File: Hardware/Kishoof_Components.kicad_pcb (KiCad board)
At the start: 2 copper layers, 76 parts, among them J1 SWD_Header, J2 Eurorack_10_pin_power, J3 Conn_01x08_Pin, J4 Conn_01x08_Pin, J5 Conn_01x08_Pin, J6 Conn_01x08_Pin, U1 STM32H7B0VBTx, U2 PCM5100APW, U3 TPS561201, U4 LT1117-3.3, U6 MX25LM51245G, U7 MCP6004, U8 TL072, U9 STF202-22T1G

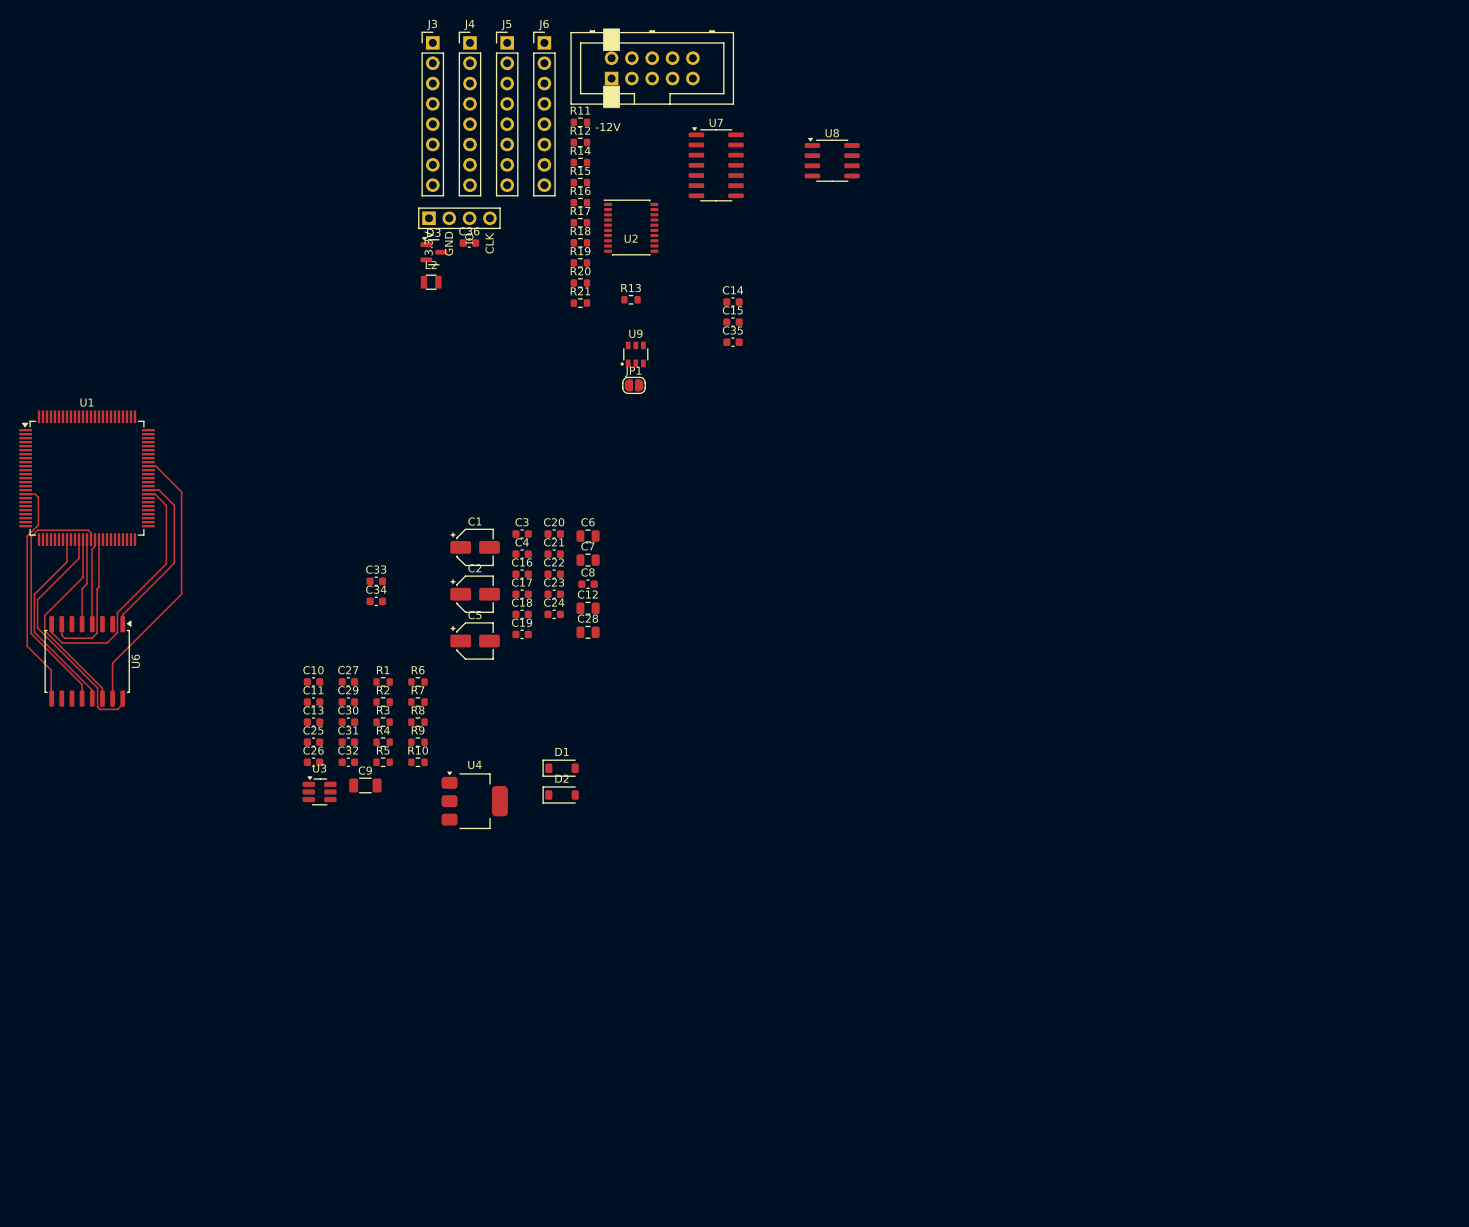
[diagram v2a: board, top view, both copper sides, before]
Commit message: Updating component and panel PCBs
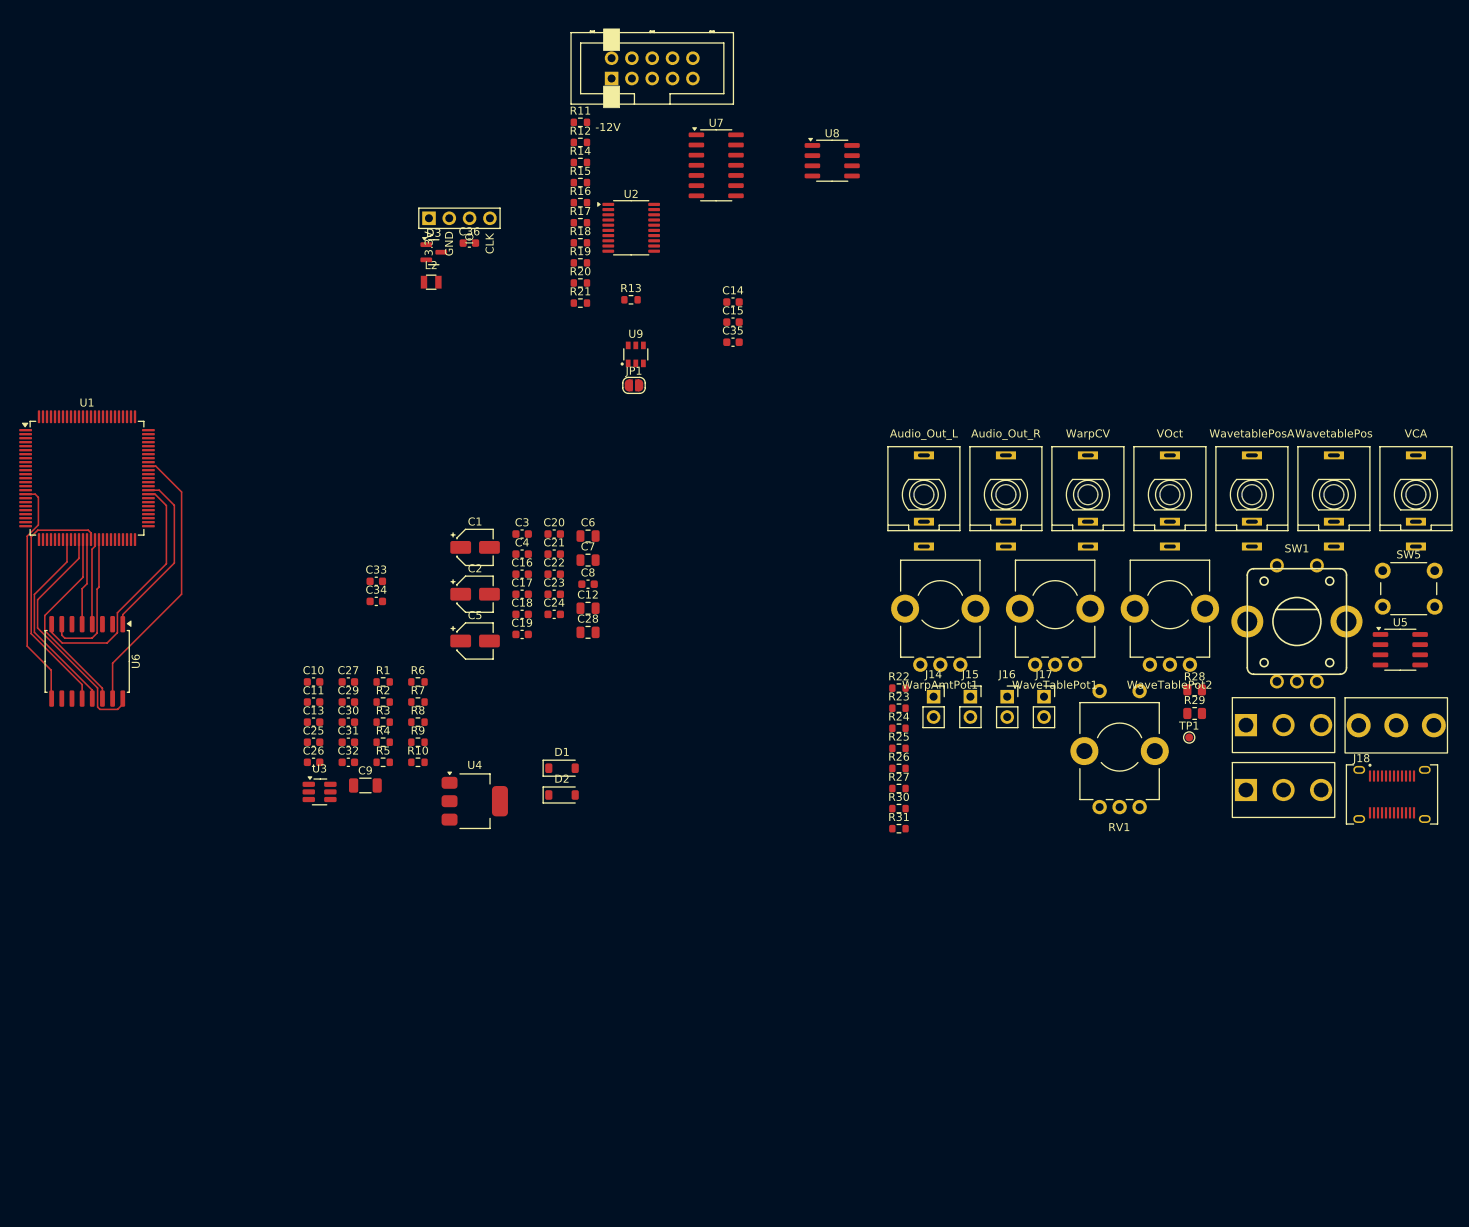
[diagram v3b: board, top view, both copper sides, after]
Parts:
- removed J3, J4, J5, J6: Conn_01x08_Pin, Connector_PinHeader_2.54mm:PinHeader_1x08_P2.54mm_Vertical
- added J10: VOct, Custom_Footprints:THONKICONN_hole, F.Cu at (178.1, 60.5)
- added J11: WavetablePosA, Custom_Footprints:THONKICONN_hole, F.Cu at (188.4, 60.5)
- added J12: WavetablePos, Custom_Footprints:THONKICONN_hole, F.Cu at (198.6, 60.5)
- added J13: VCA, Custom_Footprints:THONKICONN_hole, F.Cu at (208.9, 60.5)
- added J14: Conn_01x02_Socket, Connector_PinSocket_2.54mm:PinSocket_1x02_P2.54mm_Vertical, F.Cu at (148.6, 85.7)
- added J15: Conn_01x02_Socket, Connector_PinSocket_2.54mm:PinSocket_1x02_P2.54mm_Vertical, F.Cu at (153.2, 85.7)
- added J16: Conn_01x02_Socket, Connector_PinSocket_2.54mm:PinSocket_1x02_P2.54mm_Vertical, F.Cu at (157.8, 85.7)
- added J17: Conn_01x02_Socket, Connector_PinSocket_2.54mm:PinSocket_1x02_P2.54mm_Vertical, F.Cu at (162.4, 85.7)
- added J18: USB_C_Receptacle, Custom_Footprints:USB_C_Receptacle_Amphenol_12401951E412A, F.Cu at (205.9, 97.9)
- added J7: Audio_Out_L, Custom_Footprints:THONKICONN_hole, F.Cu at (147.4, 60.5)
- added J8: Audio_Out_R, Custom_Footprints:THONKICONN_hole, F.Cu at (157.6, 60.5)
- added J9: WarpCV, Custom_Footprints:THONKICONN_hole, F.Cu at (167.9, 60.5)
- added R22: 75k, Resistor_SMD:R_0603_1608Metric, F.Cu at (144.3, 84.6)
- added R23: 91k, Resistor_SMD:R_0603_1608Metric, F.Cu at (144.3, 87.2)
- added R24: 47k, Resistor_SMD:R_0603_1608Metric, F.Cu at (144.3, 89.7)
- added R25: 75k, Resistor_SMD:R_0603_1608Metric, F.Cu at (144.3, 92.2)
- added R26: 91k, Resistor_SMD:R_0603_1608Metric, F.Cu at (144.3, 94.7)
- added R27: 47k, Resistor_SMD:R_0603_1608Metric, F.Cu at (144.3, 97.2)
- added R28: 5k1, Resistor_SMD:R_0805_2012Metric, F.Cu at (181.2, 84.9)
- added R29: 5k1, Resistor_SMD:R_0805_2012Metric, F.Cu at (181.2, 87.8)
- added R30: 10k, Resistor_SMD:R_0603_1608Metric, F.Cu at (144.3, 99.7)
- added R31: 10k, Resistor_SMD:R_0603_1608Metric, F.Cu at (144.3, 102.2)
- added RV1: WarpTypePot, Custom_Footprints:Bourns_Switch_Potentiometer, F.Cu at (171.8, 92.0)
- added SW1: Encoder, Custom_Footprints:Encoder, F.Cu at (194.0, 76.3)
- added SW2: Mode_Switch, Custom_Footprints:SPDT_Miniature, F.Cu at (206.4, 89.3)
- added SW3: Octave_Switch, Custom_Footprints:SP3T_Mini_Switch, F.Cu at (192.3, 89.3)
- added SW4: ChB_Output, Custom_Footprints:SP3T_Mini_Switch, F.Cu at (192.3, 97.4)
- added SW5: SW_Push, Custom_Footprints:SW_PUSH_6mm_aligned, F.Cu at (208.0, 72.2)
- added TP1: TestPoint, TestPoint:TestPoint_Pad_D1.0mm, F.Cu at (180.6, 90.8)
- added U5: MCP6002, Package_SO:SOIC-8_3.9x4.9mm_P1.27mm, F.Cu at (206.9, 79.8)
- added WarpAmtPot1: B10k, Custom_Footprints:Alpha_9mm_Potentiometer_Aligned, F.Cu at (149.4, 74.2)
- added WaveTablePot1: B10k, Custom_Footprints:Alpha_9mm_Potentiometer_Aligned, F.Cu at (163.8, 74.2)
- added WaveTablePot2: B10k, Custom_Footprints:Alpha_9mm_Potentiometer_Aligned, F.Cu at (178.1, 74.2)
- C9: footprint Resistor_SMD:R_1206_3216Metric -> Capacitor_SMD:C_1206_3216Metric
- U2: footprint Custom_Footprints:SSOP-20_4.4x6.5mm_Pitch0.65mm_Round_Pads -> Package_SO:TSSOP-20_4.4x6.5mm_P0.65mm
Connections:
- net /WaveTable_Pos_A_CV renamed /WavetablePosA_CV
- net /WaveTable_Pos_B_CV renamed /WavetablePosB_CV
- U1 pad 29: unconnected-(U1-PA5-Pad29) -> /WarpCV
- U1 pad 30: unconnected-(U1-PA6-Pad30) -> /WARP_AMT_POT
- U1 pad 31: unconnected-(U1-PA7-Pad31) -> /VcaCV
- U1 pad 34: unconnected-(U1-PB0-Pad34) -> /Warp_Type_Pot
- U1 pad 42: unconnected-(U1-PE12-Pad42) -> /ChB_Mix
- U1 pad 43: unconnected-(U1-PE13-Pad43) -> /ChB_RM
- U1 pad 44: unconnected-(U1-PE14-Pad44) -> /WARP_BIPOLAR
- U1 pad 45: unconnected-(U1-PE15-Pad45) -> /Mode
- U1 pad 62: unconnected-(U1-PD15-Pad62) -> /B_Octave_Btn1
- U1 pad 77: unconnected-(U1-PA15-Pad77) -> /LCD_SPI3_SS
- U1 pad 81: unconnected-(U1-PD0-Pad81) -> /Octave_Up
- U1 pad 82: unconnected-(U1-PD1-Pad82) -> /Octave_Down
- U1 pad 92: unconnected-(U1-PB6-Pad92) -> /Warp_Polarity_Btn
- U7 pad 12: (no net) -> GND
- U7 pad 13: (no net) -> Net-(U7D--)
- U7 pad 14: (no net) -> /WarpCV

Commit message: Schematic updates
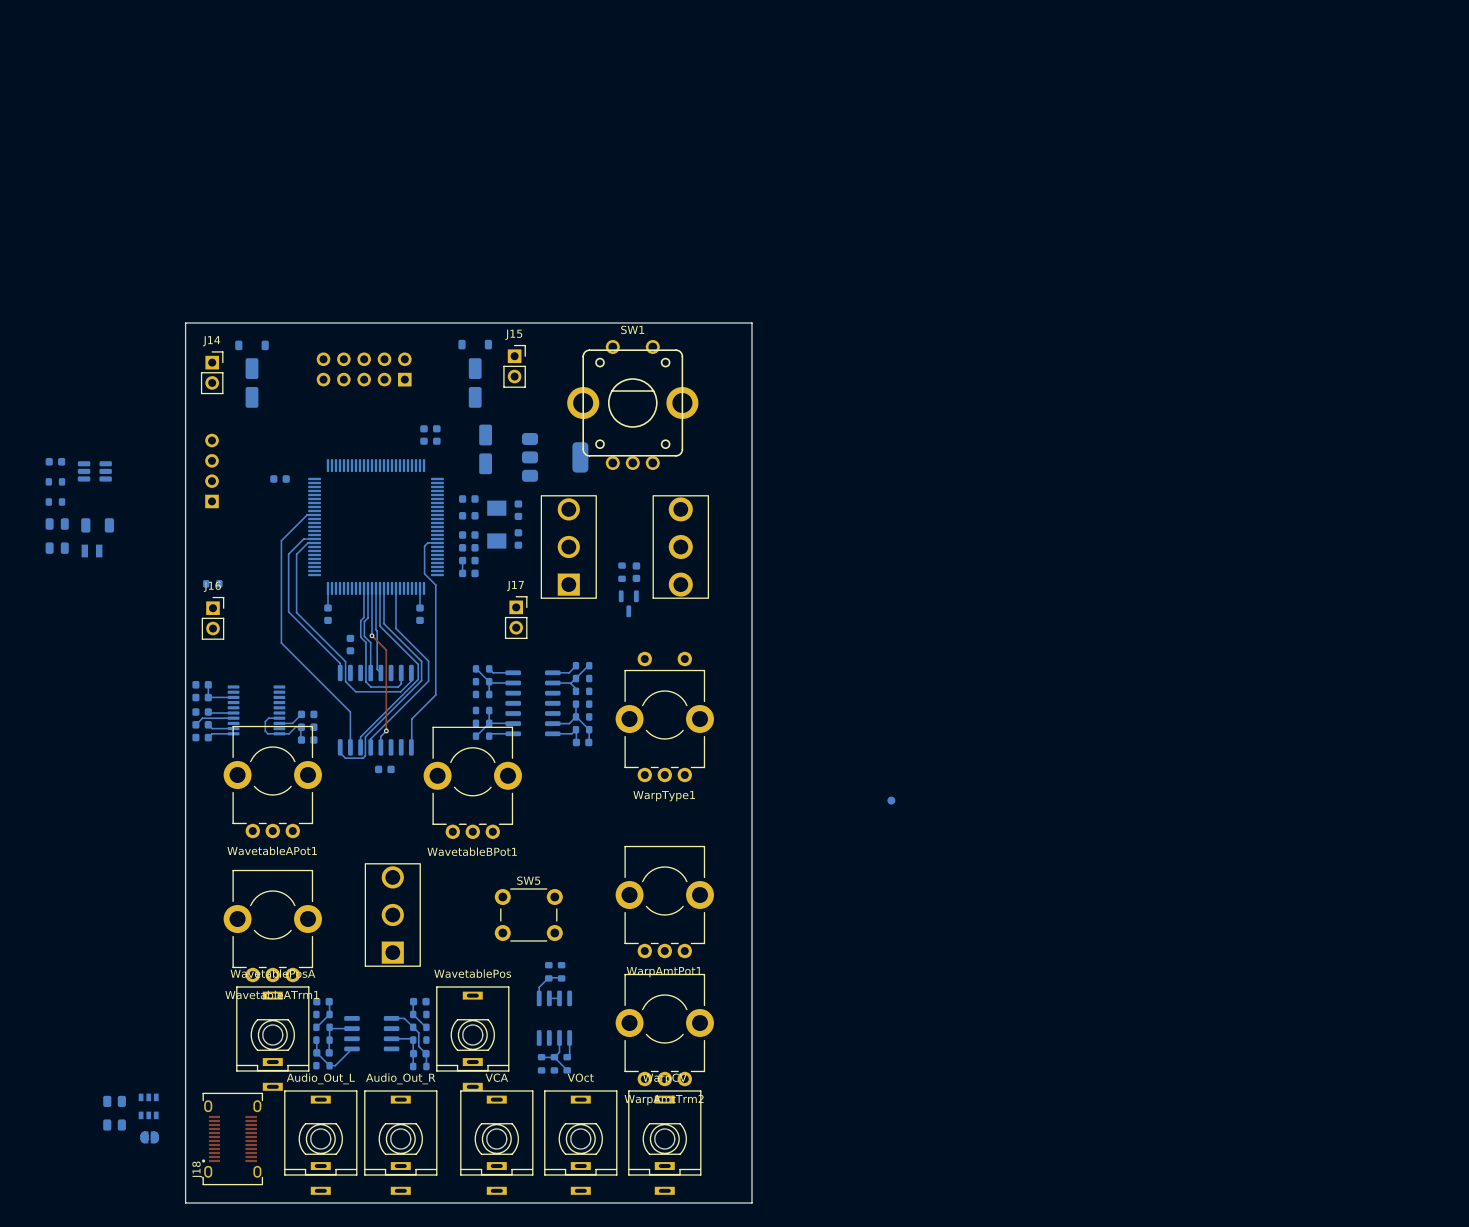
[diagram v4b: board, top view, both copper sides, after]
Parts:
- added WarpAmtTrm2: B10k, Custom_Footprints:Alpha_9mm_Potentiometer_Aligned, F.Cu at (115.0, 126.0)
- added WavetableATrm1: B10k, Custom_Footprints:Alpha_9mm_Potentiometer_Aligned, F.Cu at (66.0, 113.0)
- added Y1: 8MHz 20pF, Crystal:Crystal_SMD_Abracon_ABM3-2Pin_5.0x3.2mm, B.Cu at (94.0, 64.2)
- C1, C10, C11, C13, C14, C15, C16, C17, C18, C19, C2, C20, C21, C22, C23, C24, C25, C26, C27, C29, C3, C30, C31, C32, C33, C34, C35, C36, C4, C5, C6, C7, C8, C9, D1, D2, D3, J1, J2, JP1, L2, R1, R10, R11, R12, R13, R14, R15, R16, R17, R18, R19, R2, R20, R21, R22, R23, R24, R25, R26, R27, R28, R29, R3, R30, R31, R4, R5, R6, R7, R8, R9, TP1, U1, U2, U3, U4, U5, U6, U7, U8, U9: moved to B.Cu
- C12, C28: footprint Capacitor_SMD:C_0805_2012Metric -> Capacitor_SMD:C_0603_1608Metric; moved to B.Cu
- moved J18 151.2 mm to (61.0, 141.0), turned to 90 degrees
- moved R28 144.5 mm to (46.2, 136.3), turned to 180 degrees
- moved R29 144.5 mm to (46.2, 139.2), turned to 180 degrees
- moved J13 140.3 mm to (94.0, 141.0)
- moved J11 139.8 mm to (66.0, 128.0)
- moved J12 127.1 mm to (91.0, 128.0)
- moved U8 123.4 mm to (78.4, 127.8)
- moved SW5 117.3 mm to (98.0, 113.0)
- moved U5 115.3 mm to (101.2, 125.9), turned to 90 degrees
- moved WavetableAPot1 114.1 mm to (66.0, 95.0)
- moved SW4 112.4 mm to (81.0, 113.0), turned to 90 degrees
- moved U9 112.0 mm to (50.5, 136.9), turned to 180 degrees
- moved JP1 111.8 mm to (50.6, 140.8), turned to 180 degrees
- moved J8 110.5 mm to (82.0, 141.0)
- moved J7 110.3 mm to (72.0, 141.0)
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- renumbered RV1 to WarpType1, WaveTablePot2 to WavetableAPot1, WaveTablePot1 to WavetableBPot1
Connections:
- U1 pad 15: unconnected-(U1-PC0-Pad15) -> /WARP_AMT_TRM
- U1 pad 16: unconnected-(U1-PC1-Pad16) -> /WAVETABLE_POS_A_TRM
- U1 pad 46: /OCTOSPIM_P1_NCS -> unconnected-(U1-PB10-Pad46)
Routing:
- net /OCTOSPIM_P1_IO6: track 31.7 -> 20.9 mm, vias 0 -> 2
- net +3.3VA: track 0.00 -> 10.2 mm
- net +3V3: track 0.00 -> 9.97 mm
- net Net-(U7B--): track 0.00 -> 8.78 mm
- net Net-(U8B-+): track 0.00 -> 8.74 mm
- net Net-(C31-Pad1): track 0.00 -> 7.55 mm
- net Net-(U7D--): track 0.00 -> 6.98 mm
- net Net-(U7C--): track 0.00 -> 6.93 mm
- net Net-(U7A--): track 0.00 -> 6.81 mm
- net Net-(U5A--): track 0.00 -> 6.60 mm
- net Net-(C32-Pad1): track 0.00 -> 6.11 mm
- net Net-(U8A-+): track 0.00 -> 6.09 mm
- net Net-(U2-CAPM): track 0.00 -> 5.05 mm
- net +3.3V: track 0.00 -> 4.90 mm
- net Net-(U5B-+): track 0.00 -> 4.77 mm
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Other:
- board outline added: 70.8 x 110 mm
- copper layers 2 -> 4
